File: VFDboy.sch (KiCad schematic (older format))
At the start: 34 parts, among them J1 AVR-ISP-6, SW1 SW_Push, SW2 SW_Push, SW3 SW_Push, SW4 SW_Push, SW5 SW_Push, SW6 SW_Push, SW7 RESET, U1 ATmega32U4-MU, U2 SSD1306_VFD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

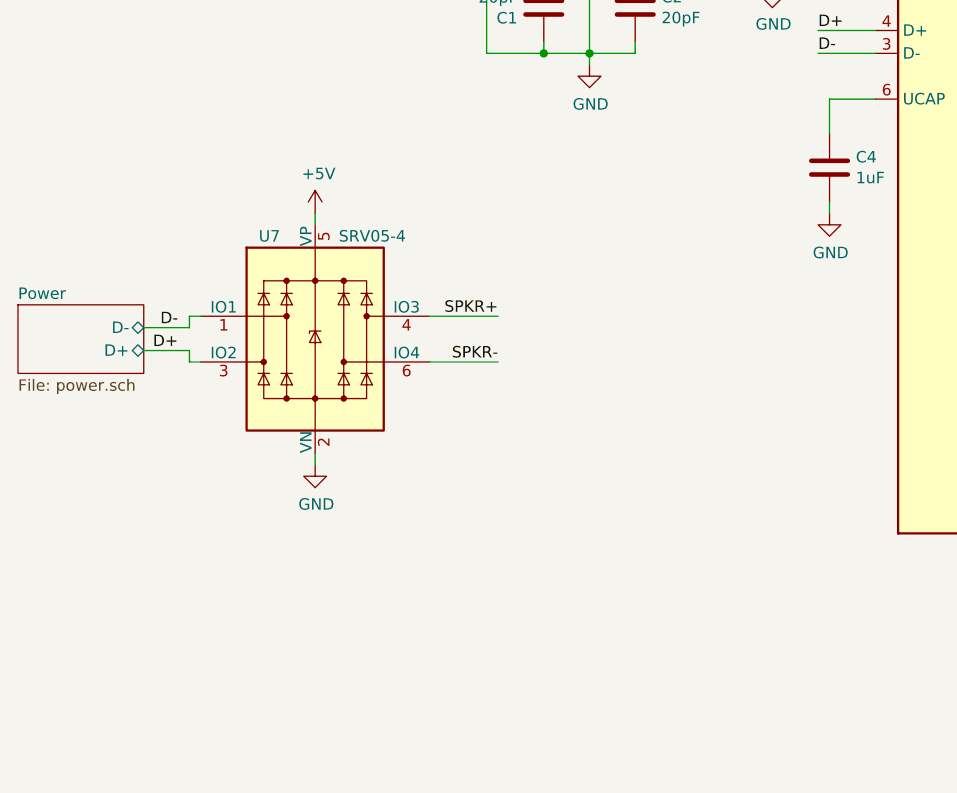
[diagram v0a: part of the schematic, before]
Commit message: Add self-programming capability
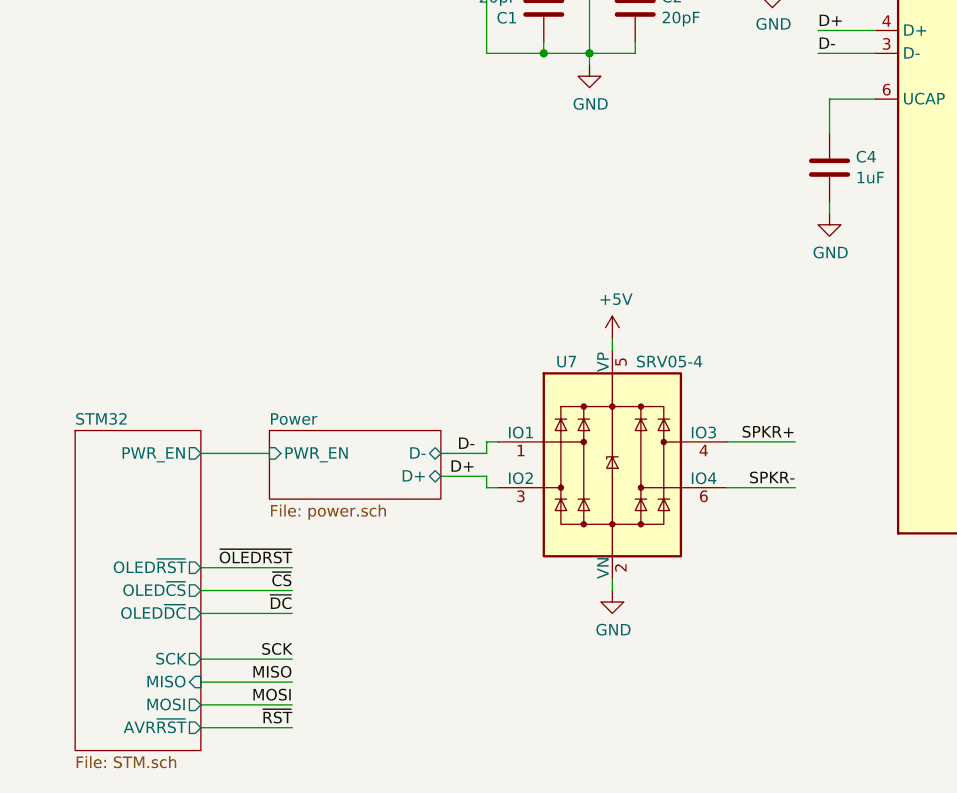
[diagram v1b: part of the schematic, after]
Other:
- moved on the sheet: U7
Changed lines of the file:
@@
 $Descr A4 11693 8268
 encoding utf-8
-Sheet 1 3
+Sheet 1 4
 Title ""
 Date ""
@@
 Text Label 9500 3450 0    50   ~ 0
 MISO
-$Sheet
-S 950  4350 550  300
-U 6051E9DC
-F0 "Power" 50
-F1 "power.sch" 50
-F2 "D-" B R 1500 4450 50
-F3 "D+" B R 1500 4550 50
-$EndSheet
-Text Label 1650 4450 2    50   ~ 0
+Text Label 2950 5000 2    50   ~ 0
 D-
-Text Label 1650 4550 2    50   ~ 0
+Text Label 2950 5100 2    50   ~ 0
 D+
 $Comp
@@
 L Power_Protection:SRV05-4 U7
 U 1 1 607CF2D7
-P 2250 4500
-F 0 "U7" H 2050 4950 50  0000 C CNN
-F 1 "SRV05-4" H 2500 4950 50  0000 C CNN
-F 2 "Package_TO_SOT_SMD:SOT-23-6" H 2950 4050 50  0001 C CNN
-F 3 "http://www.onsemi.com/pub/Collateral/SRV05-4-D.PDF" H 2250 4500 50  0001 C CNN
-F 4 "C85364" H 2250 4500 50  0001 C CNN "LCSC"
-	1    2250 4500
-	1    0    0    -1
-$EndComp
-Wire Wire Line
-	2250 3950 2250 4000
+P 3550 5050
+F 0 "U7" H 3350 5500 50  0000 C CNN
+F 1 "SRV05-4" H 3800 5500 50  0000 C CNN
+F 2 "Package_TO_SOT_SMD:SOT-23-6" H 4250 4600 50  0001 C CNN
+F 3 "http://www.onsemi.com/pub/Collateral/SRV05-4-D.PDF" H 3550 5050 50  0001 C CNN
+F 4 "C85364" H 3550 5050 50  0001 C CNN "LCSC"
+	1    3550 5050
+	1    0    0    -1
+$EndComp
+Wire Wire Line
+	3550 4500 3550 4550
 $Comp
 L power:GND #PWR0101
 U 1 1 60812A04
-P 2250 5050
-F 0 "#PWR0101" H 2250 4800 50  0001 C CNN
-F 1 "GND" H 2255 4877 50  0000 C CNN
-F 2 "" H 2250 5050 50  0001 C CNN
-F 3 "" H 2250 5050 50  0001 C CNN
-	1    2250 5050
-	1    0    0    -1
-$EndComp
-Wire Wire Line
-	2250 5050 2250 5000
-Wire Wire Line
-	1700 4450 1700 4400
-Wire Wire Line
-	1700 4400 1750 4400
-Wire Wire Line
-	1500 4450 1700 4450
-Wire Wire Line
-	1700 4550 1700 4600
-Wire Wire Line
-	1700 4600 1750 4600
-Wire Wire Line
-	1500 4550 1700 4550
-Text Label 3050 4400 2    50   ~ 0
+P 3550 5600
+F 0 "#PWR0101" H 3550 5350 50  0001 C CNN
+F 1 "GND" H 3555 5427 50  0000 C CNN
+F 2 "" H 3550 5600 50  0001 C CNN
+F 3 "" H 3550 5600 50  0001 C CNN
+	1    3550 5600
+	1    0    0    -1
+$EndComp
+Wire Wire Line
+	3550 5600 3550 5550
+Wire Wire Line
+	3000 5000 3000 4950
+Wire Wire Line
+	3000 4950 3050 4950
+Wire Wire Line
+	2800 5000 3000 5000
+Wire Wire Line
+	3000 5100 3000 5150
+Wire Wire Line
+	3000 5150 3050 5150
+Wire Wire Line
+	2800 5100 3000 5100
+Text Label 4350 4950 2    50   ~ 0
 SPKR+
-Text Label 3050 4600 2    50   ~ 0
+Text Label 4350 5150 2    50   ~ 0
 SPKR-
 Wire Wire Line
-	2750 4400 3050 4400
-Wire Wire Line
-	3050 4600 2750 4600
+	4050 4950 4350 4950
+Wire Wire Line
+	4350 5150 4050 5150
 $Comp
 L Device:R R21
@@
 L power:+5V #PWR0102
 U 1 1 6087AF0F
-P 2250 3950
-F 0 "#PWR0102" H 2250 3800 50  0001 C CNN
-F 1 "+5V" H 2265 4123 50  0000 C CNN
-F 2 "" H 2250 3950 50  0001 C CNN
-F 3 "" H 2250 3950 50  0001 C CNN
-	1    2250 3950
+P 3550 4500
+F 0 "#PWR0102" H 3550 4350 50  0001 C CNN
+F 1 "+5V" H 3565 4673 50  0000 C CNN
+F 2 "" H 3550 4500 50  0001 C CNN
+F 3 "" H 3550 4500 50  0001 C CNN
+	1    3550 4500
 	1    0    0    -1
 $EndComp
@@
 Wire Wire Line
 	4000 2150 4250 2150
+$Sheet
+S 2050 4900 750  300
+U 6051E9DC
+F0 "Power" 50
+F1 "power.sch" 50
+F2 "D-" B R 2800 5000 50
+F3 "D+" B R 2800 5100 50
+F4 "PWR_EN" I L 2050 5000 50
+$EndSheet
+Wire Wire Line
+	1750 5000 2050 5000
+Text Label 2150 6200 2    50   ~ 0
+~RST
+Text Label 2150 5900 2    50   ~ 0
+SCK
+Text Label 2150 6100 2    50   ~ 0
+MOSI
+Text Label 2150 6000 2    50   ~ 0
+MISO
+$Sheet
+S 1200 4900 550  1400
+U 60CF39C0
+F0 "STM32" 50
+F1 "STM.sch" 50
+F2 "PWR_EN" O R 1750 5000 50
+F3 "SCK" O R 1750 5900 50
+F4 "MISO" I R 1750 6000 50
+F5 "MOSI" O R 1750 6100 50
+F6 "AVR~RST" O R 1750 6200 50
+F7 "OLED~RST" O R 1750 5500 50
+F8 "OLED~CS" O R 1750 5600 50
+F9 "OLED~DC" O R 1750 5700 50
+$EndSheet
+Text Label 2150 5500 2    50   ~ 0
+~OLEDRST
+Text Label 2150 5700 2    50   ~ 0
+~DC
+Text Label 2150 5600 2    50   ~ 0
+~CS
+Wire Wire Line
+	1750 6100 2150 6100
+Wire Wire Line
+	1750 6000 2150 6000
+Wire Wire Line
+	1750 5900 2150 5900
+Wire Wire Line
+	2150 5700 1750 5700
+Wire Wire Line
+	2150 5600 1750 5600
+Wire Wire Line
+	2150 5500 1750 5500
+Wire Wire Line
+	2150 6200 1750 6200
 $EndSCHEMATC

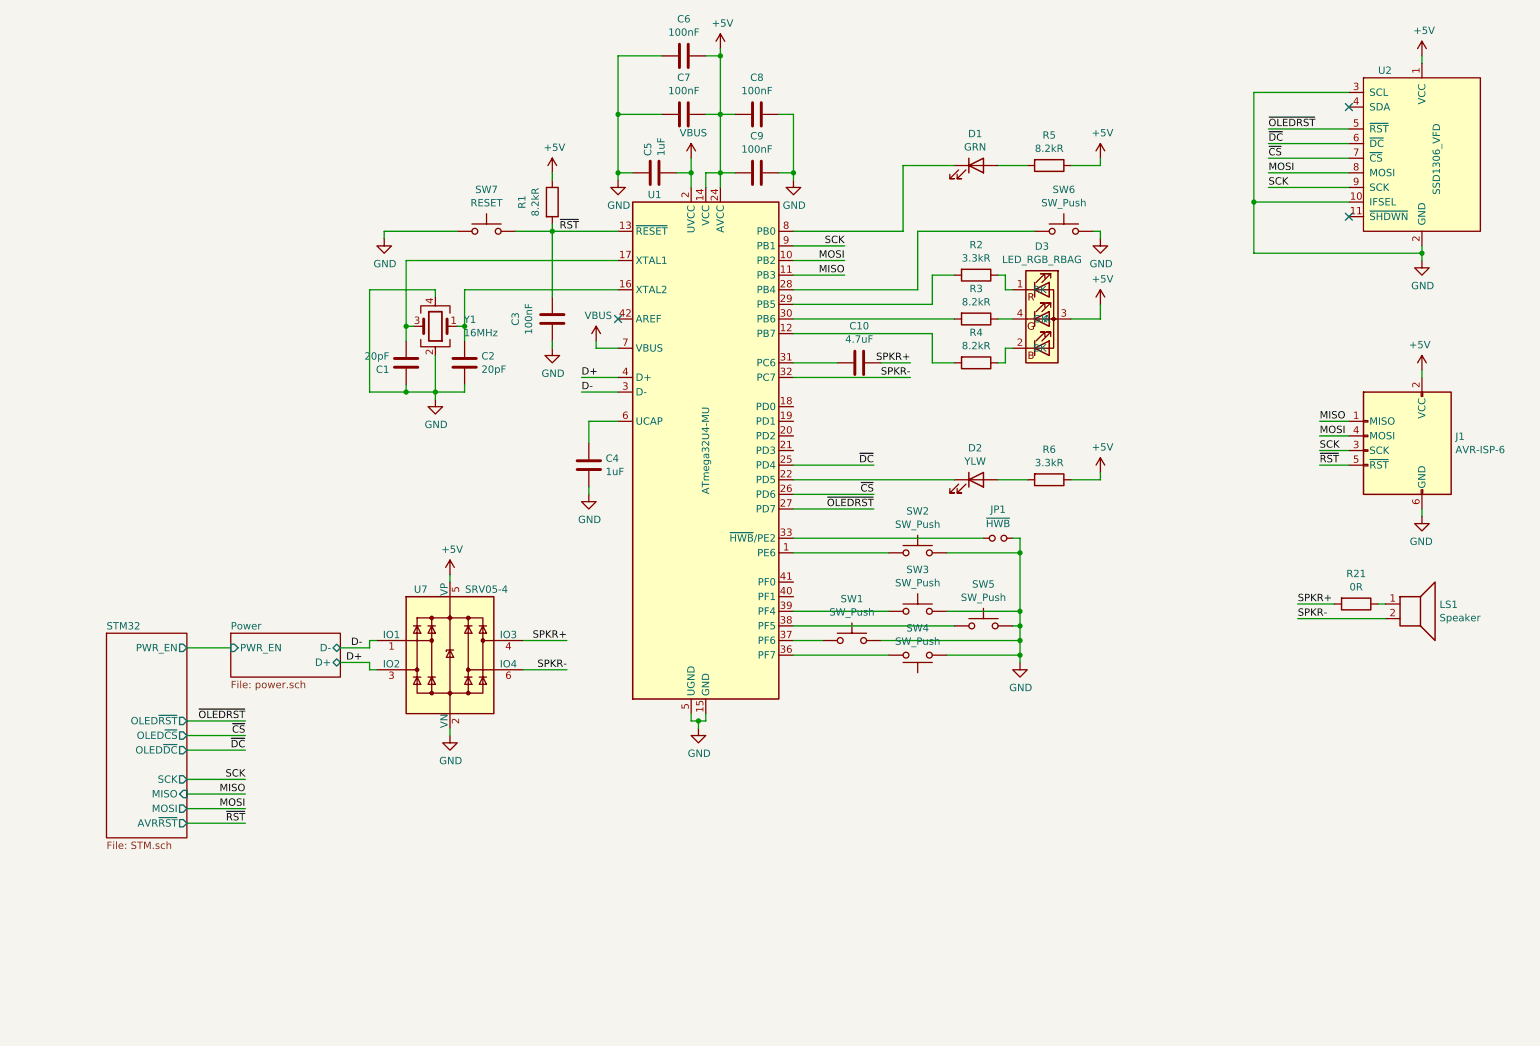
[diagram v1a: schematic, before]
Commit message: Add charge state/current sensing and VBUS wakeup source
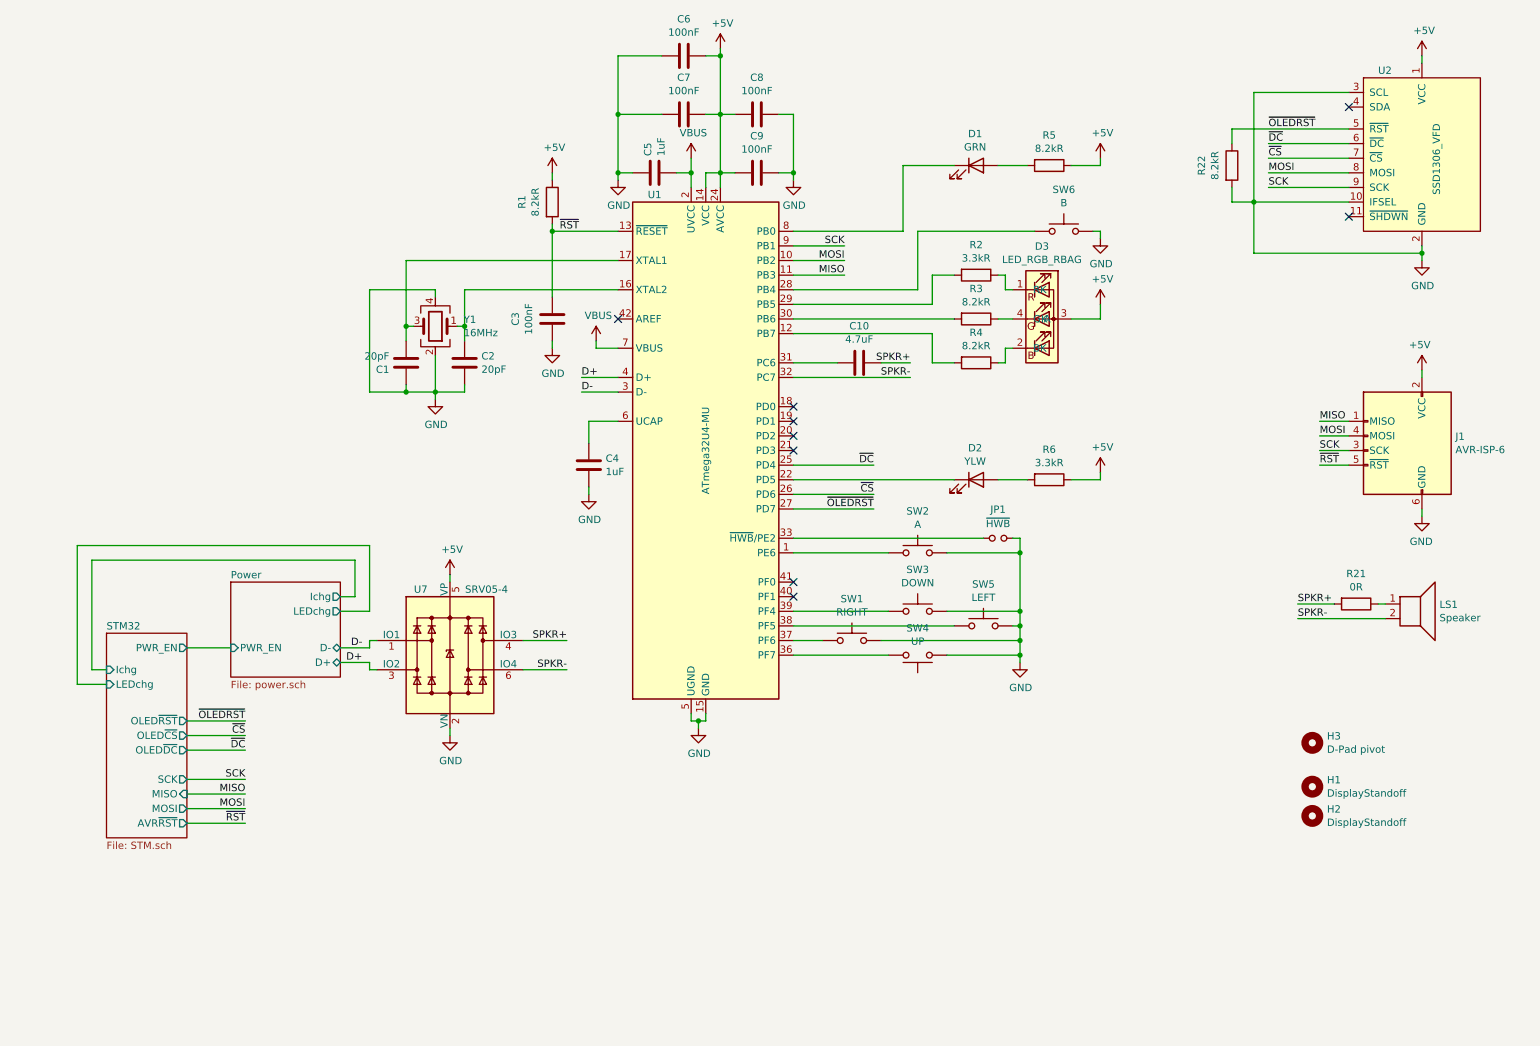
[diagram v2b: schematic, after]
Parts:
- removed SW7: RESET, Button_Carbon:Button_Carbon_5mm, symbol Switch:SW_Push
- added H1, H2: DisplayStandoff, MountingHole:MountingHole_2.7mm_M2.5, symbol Mechanical:MountingHole
- added H3: D-Pad pivot, MountingHole:MountingHole_5.5mm, symbol Mechanical:MountingHole
- added R22: 8.2kR, Resistor_SMD:R_0402_1005Metric, symbol Device:R
- SW1: value SW_Push -> RIGHT
- SW2: value SW_Push -> A
- SW3: value SW_Push -> DOWN
- SW4: value SW_Push -> UP
- SW5: value SW_Push -> LEFT
- SW6: value SW_Push -> B
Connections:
- net GND: now also R22.2
- net ~OLEDRST: now also R22.1
- no-connect marks 3 -> 9
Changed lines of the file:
@@
 P 6750 5050
 F 0 "SW4" H 6750 4865 50  0000 C CNN
-F 1 "SW_Push" H 6750 4956 50  0000 C CNN
+F 1 "UP" H 6750 4956 50  0000 C CNN
 F 2 "Button_Carbon:Button_Carbon_5mm" H 6750 5250 50  0001 C CNN
 F 3 "~" H 6750 5250 50  0001 C CNN
@@
 P 7200 4850
 F 0 "SW5" H 7200 5135 50  0000 C CNN
-F 1 "SW_Push" H 7200 5044 50  0000 C CNN
+F 1 "LEFT" H 7200 5044 50  0000 C CNN
 F 2 "Button_Carbon:Button_Carbon_5mm" H 7200 5050 50  0001 C CNN
 F 3 "~" H 7200 5050 50  0001 C CNN
@@
 P 6300 4950
 F 0 "SW1" H 6300 5235 50  0000 C CNN
-F 1 "SW_Push" H 6300 5144 50  0000 C CNN
+F 1 "RIGHT" H 6300 5144 50  0000 C CNN
 F 2 "Button_Carbon:Button_Carbon_5mm" H 6300 5150 50  0001 C CNN
 F 3 "~" H 6300 5150 50  0001 C CNN
@@
 P 6750 4750
 F 0 "SW3" H 6750 5035 50  0000 C CNN
-F 1 "SW_Push" H 6750 4944 50  0000 C CNN
+F 1 "DOWN" H 6750 4944 50  0000 C CNN
 F 2 "Button_Carbon:Button_Carbon_5mm" H 6750 4950 50  0001 C CNN
 F 3 "~" H 6750 4950 50  0001 C CNN
@@
 P 6750 4350
 F 0 "SW2" H 6750 4635 50  0000 C CNN
-F 1 "SW_Push" H 6750 4544 50  0000 C CNN
+F 1 "A" H 6750 4544 50  0000 C CNN
 F 2 "Button_Carbon:Button_Carbon_5mm" H 6750 4550 50  0001 C CNN
 F 3 "~" H 6750 4550 50  0001 C CNN
@@
 P 7750 2150
 F 0 "SW6" H 7750 2435 50  0000 C CNN
-F 1 "SW_Push" H 7750 2344 50  0000 C CNN
+F 1 "B" H 7750 2344 50  0000 C CNN
 F 2 "Button_Carbon:Button_Carbon_5mm" H 7750 2350 50  0001 C CNN
 F 3 "~" H 7750 2350 50  0001 C CNN
@@
 Wire Wire Line
 	4250 2150 4250 2600
-$Comp
-L Device:R R1
-U 1 1 5FFCEB8B
-P 4250 1950
-F 0 "R1" V 4043 1950 50  0000 C CNN
-F 1 "8.2kR" V 4134 1950 50  0000 C CNN
-F 2 "Resistor_SMD:R_0402_1005Metric" V 4180 1950 50  0001 C CNN
-F 3 "~" H 4250 1950 50  0001 C CNN
-F 4 "C25924" V 4250 1950 50  0001 C CNN "LCSC"
-	1    4250 1950
-	1    0    0    -1
-$EndComp
 Wire Wire Line
 	4250 2100 4250 2150
@@
 Text Label 6250 2450 2    50   ~ 0
 MISO
-Wire Wire Line
-	9700 1450 9150 1450
 Text Label 9150 1450 0    50   ~ 0
 ~OLEDRST
@@
 	1    0    0    -1
 $EndComp
-$Comp
-L Switch:SW_Push SW7
-U 1 1 6087BC77
-P 3800 2150
-F 0 "SW7" H 3800 2435 50  0000 C CNN
-F 1 "RESET" H 3800 2344 50  0000 C CNN
-F 2 "Button_Carbon:Button_Carbon_5mm" H 3800 2350 50  0001 C CNN
-F 3 "~" H 3800 2350 50  0001 C CNN
-	1    3800 2150
-	1    0    0    -1
-$EndComp
-$Comp
-L power:GND #PWR0103
-U 1 1 60882911
-P 3100 2200
-F 0 "#PWR0103" H 3100 1950 50  0001 C CNN
-F 1 "GND" H 3105 2027 50  0000 C CNN
-F 2 "" H 3100 2200 50  0001 C CNN
-F 3 "" H 3100 2200 50  0001 C CNN
-	1    3100 2200
-	1    0    0    -1
-$EndComp
-Wire Wire Line
-	3600 2150 3100 2150
-Wire Wire Line
-	3100 2150 3100 2200
-Wire Wire Line
-	4000 2150 4250 2150
 $Sheet
-S 2050 4900 750  300
+S 2050 4550 750  650
 U 6051E9DC
 F0 "Power" 50
@@
 F3 "D+" B R 2800 5100 50
 F4 "PWR_EN" I L 2050 5000 50
+F5 "Ichg" O R 2800 4650 50
+F6 "LEDchg" O R 2800 4750 50
 $EndSheet
 Wire Wire Line
@@
 F8 "OLED~CS" O R 1750 5600 50
 F9 "OLED~DC" O R 1750 5700 50
+F10 "Ichg" I L 1200 5150 50
+F11 "LEDchg" I L 1200 5250 50
 $EndSheet
 Text Label 2150 5500 2    50   ~ 0
@@
 Wire Wire Line
 	2150 6200 1750 6200
+$Comp
+L Mechanical:MountingHole H1
+U 1 1 60EAD0C2
+P 9450 5950
+F 0 "H1" H 9550 5996 50  0000 L CNN
+F 1 "DisplayStandoff" H 9550 5905 50  0000 L CNN
+F 2 "MountingHole:MountingHole_2.7mm_M2.5" H 9450 5950 50  0001 C CNN
+F 3 "~" H 9450 5950 50  0001 C CNN
+	1    9450 5950
+	1    0    0    -1
+$EndComp
+$Comp
+L Mechanical:MountingHole H2
+U 1 1 60EAD556
+P 9450 6150
+F 0 "H2" H 9550 6196 50  0000 L CNN
+F 1 "DisplayStandoff" H 9550 6105 50  0000 L CNN
+F 2 "MountingHole:MountingHole_2.7mm_M2.5" H 9450 6150 50  0001 C CNN
+F 3 "~" H 9450 6150 50  0001 C CNN
+	1    9450 6150
+	1    0    0    -1
+$EndComp
+$Comp
+L Device:R R1
+U 1 1 5FFCEB8B
+P 4250 1950
+F 0 "R1" V 4043 1950 50  0000 C CNN
+F 1 "8.2kR" V 4134 1950 50  0000 C CNN
+F 2 "Resistor_SMD:R_0402_1005Metric" V 4180 1950 50  0001 C CNN
+F 3 "~" H 4250 1950 50  0001 C CNN
+F 4 "C25924" V 4250 1950 50  0001 C CNN "LCSC"
+	1    4250 1950
+	1    0    0    -1
+$EndComp
+$Comp
+L Device:R R22
+U 1 1 60EC7A43
+P 8900 1700
+F 0 "R22" V 8693 1700 50  0000 C CNN
+F 1 "8.2kR" V 8784 1700 50  0000 C CNN
+F 2 "Resistor_SMD:R_0402_1005Metric" V 8830 1700 50  0001 C CNN
+F 3 "~" H 8900 1700 50  0001 C CNN
+F 4 "C25924" V 8900 1700 50  0001 C CNN "LCSC"
+	1    8900 1700
+	1    0    0    -1
+$EndComp
+Wire Wire Line
+	8900 1450 8900 1550
+Wire Wire Line
+	8900 1450 9700 1450
+Wire Wire Line
+	9050 1950 8900 1950
+Wire Wire Line
+	8900 1950 8900 1850
+NoConn ~ 5900 3350
+NoConn ~ 5900 3450
+NoConn ~ 5900 3550
+NoConn ~ 5900 3650
+NoConn ~ 5900 4550
+NoConn ~ 5900 4650
+$Comp
+L Mechanical:MountingHole H3
+U 1 1 60F25B53
+P 9450 5650
+F 0 "H3" H 9550 5696 50  0000 L CNN
+F 1 "D-Pad pivot" H 9550 5605 50  0000 L CNN
+F 2 "MountingHole:MountingHole_5.5mm" H 9450 5650 50  0001 C CNN
+F 3 "~" H 9450 5650 50  0001 C CNN
+	1    9450 5650
+	1    0    0    -1
+$EndComp
+Wire Wire Line
+	2800 4650 2900 4650
+Wire Wire Line
+	2900 4650 2900 4400
+Wire Wire Line
+	2900 4400 1100 4400
+Wire Wire Line
+	1100 4400 1100 5150
+Wire Wire Line
+	1100 5150 1200 5150
+Wire Wire Line
+	2800 4750 3000 4750
+Wire Wire Line
+	3000 4750 3000 4300
+Wire Wire Line
+	3000 4300 1000 4300
+Wire Wire Line
+	1000 4300 1000 5250
+Wire Wire Line
+	1000 5250 1200 5250
 $EndSCHEMATC

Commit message: Implement fuel gauging
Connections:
- net A: now reaches SW2.1, U1.1 (PE6)
- net B: now reaches SW6.1, U1.28 (PB4)
- net UP: now reaches SW4.2, U1.36 (PF7)
- net RIGHT: now reaches SW1.1, U1.37 (PF6)
- net LEFT: now reaches SW5.1, U1.38 (PF5)
- net DOWN: now reaches SW3.1, U1.39 (PF4)
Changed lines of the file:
@@
 F5 "Ichg" O R 2800 4650 50
 F6 "LEDchg" O R 2800 4750 50
+F7 "GAUGE_EN" I L 2050 4850 50
+F8 "SDA" B L 2050 4750 50
+F9 "SCL" I L 2050 4650 50
 $EndSheet
 Wire Wire Line
@@
 MISO
 $Sheet
-S 1200 4900 550  1400
+S 800  4550 950  1750
 U 60CF39C0
 F0 "STM32" 50
@@
 F8 "OLED~CS" O R 1750 5600 50
 F9 "OLED~DC" O R 1750 5700 50
-F10 "Ichg" I L 1200 5150 50
-F11 "LEDchg" I L 1200 5250 50
+F10 "Ichg" I L 800 4650 50
+F11 "LEDchg" I L 800 4750 50
+F12 "SCL" O R 1750 4650 50
+F13 "SDA" B R 1750 4750 50
+F14 "GAUGE_EN" O R 1750 4850 50
+F15 "A" I L 800 5000 50
+F16 "B" I L 800 5100 50
+F17 "UP" I L 800 5300 50
+F18 "LEFT" I L 800 5400 50
+F19 "DOWN" I L 800 5500 50
+F20 "RIGHT" I L 800 5600 50
 $EndSheet
 Text Label 2150 5500 2    50   ~ 0
@@
 	2900 4650 2900 4400
 Wire Wire Line
-	2900 4400 1100 4400
-Wire Wire Line
-	1100 4400 1100 5150
-Wire Wire Line
-	1100 5150 1200 5150
-Wire Wire Line
 	2800 4750 3000 4750
 Wire Wire Line
 	3000 4750 3000 4300
 Wire Wire Line
-	3000 4300 1000 4300
+	2050 4650 1750 4650
 Wire Wire Line
-	1000 4300 1000 5250
+	1750 4750 2050 4750
 Wire Wire Line
-	1000 5250 1200 5250
+	2050 4850 1750 4850
+Wire Wire Line
+	700  4400 700  4650
+Wire Wire Line
+	700  4400 2900 4400
+Wire Wire Line
+	600  4300 600  4750
+Wire Wire Line
+	600  4300 3000 4300
+Wire Wire Line
+	800  4650 700  4650
+Wire Wire Line
+	800  4750 600  4750
+Text Label 6500 4350 0    50   ~ 0
+A
+Text Label 7500 2150 0    50   ~ 0
+B
+Text Label 5900 4750 0    50   ~ 0
+DOWN
+Text Label 5900 4850 0    50   ~ 0
+LEFT
+Text Label 5900 4950 0    50   ~ 0
+RIGHT
+Text Label 5900 5050 0    50   ~ 0
+UP
+Text Label 550  5000 0    50   ~ 0
+A
+Text Label 550  5100 0    50   ~ 0
+B
+Text Label 550  5300 0    50   ~ 0
+UP
+Text Label 550  5400 0    50   ~ 0
+LEFT
+Text Label 550  5500 0    50   ~ 0
+DOWN
+Wire Wire Line
+	550  5000 800  5000
+Wire Wire Line
+	550  5100 800  5100
+Wire Wire Line
+	550  5300 800  5300
+Wire Wire Line
+	550  5400 800  5400
+Wire Wire Line
+	550  5500 800  5500
+Text Label 550  5600 0    50   ~ 0
+RIGHT
+Wire Wire Line
+	550  5600 800  5600
 $EndSCHEMATC
